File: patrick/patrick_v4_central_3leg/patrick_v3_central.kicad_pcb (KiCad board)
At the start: 2 copper layers, 47.6 x 51.7 mm, 12 parts, among them J1 Conn_02x05_Counter_Clockwise, J10 61300311121, J4 Conn_02x05_Counter_Clockwise, J5 Conn_02x05_Counter_Clockwise, J7 61300211121, J9 61300211121, U1 ZLDO1117G33TA, U3 BL652-SA-01

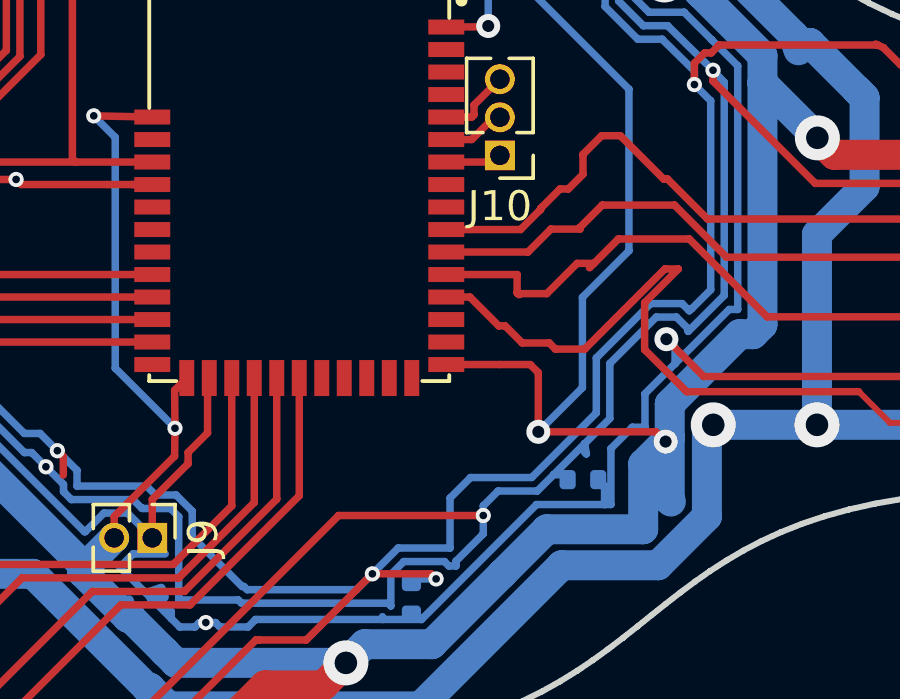
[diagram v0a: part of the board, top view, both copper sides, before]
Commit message: added IMU to 3 legged circuit
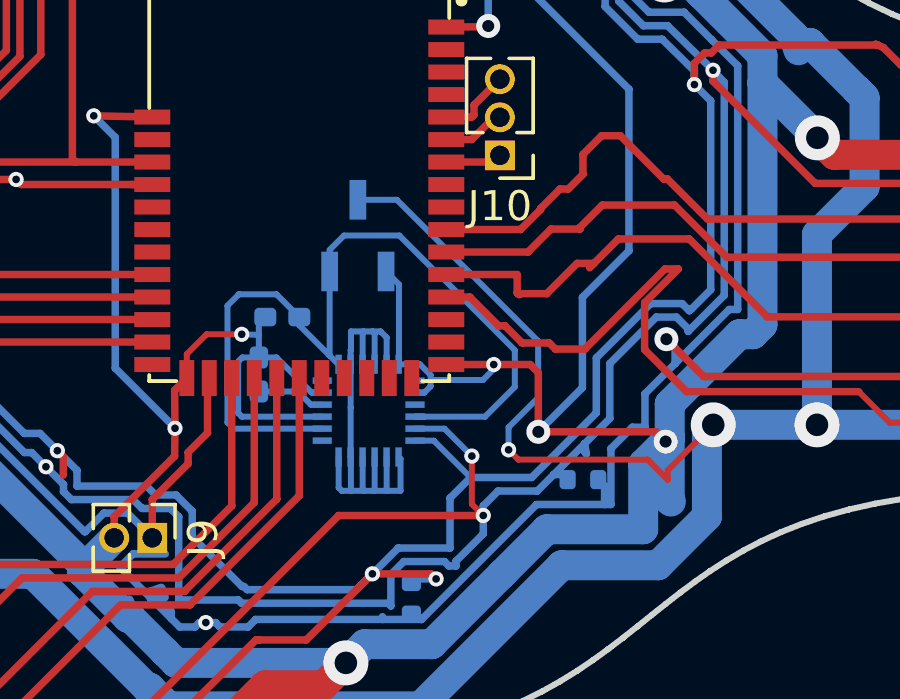
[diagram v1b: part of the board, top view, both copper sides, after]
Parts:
- added C3: C-USC0402, Capacitor_SMD:C_0402_1005Metric_Pad0.74x0.62mm_HandSolder, B.Cu at (107.5, 115.3)
- added C4: C-USC0402, Capacitor_SMD:C_0402_1005Metric_Pad0.74x0.62mm_HandSolder, B.Cu at (108.3, 113.4)
- added U2: ICM-20948, ICM-20948:QFN40P300X300X105-24N, B.Cu at (111.1, 116.5)
- added U4: MCP1703T-1802E_CB, MCP1703T-1802E_CB:SOT95P255X145-3N, B.Cu at (110.8, 110.7)
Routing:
- net Net-(C4-Pad1): track 0.00 -> 28.9 mm
- net GND: track 208.9 -> 229.6 mm, vias 10 -> 12
- net +8V: track 158.0 -> 178.2 mm, vias 2 -> 3
- net Net-(U2-Pad1): track 0.00 -> 17.4 mm
- net /SCL: track 175.5 -> 179.9 mm, vias 6 -> 7
- net /SDA: track 165.0 -> 167.4 mm
- net Net-(C3-Pad1): track 0.00 -> 2.30 mm
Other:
- net class Default: clearance 0.2 -> 0.1
- net class small added: clearance 0.1, trace_width 0.25, via_dia 0.8, via_drill 0.4
- rule trace_clearance: 0.2 -> 0.1
